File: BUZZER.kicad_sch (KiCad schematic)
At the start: 4 parts, among them Q1 AO3400A, U10 ZX-SH1.0-3PWT

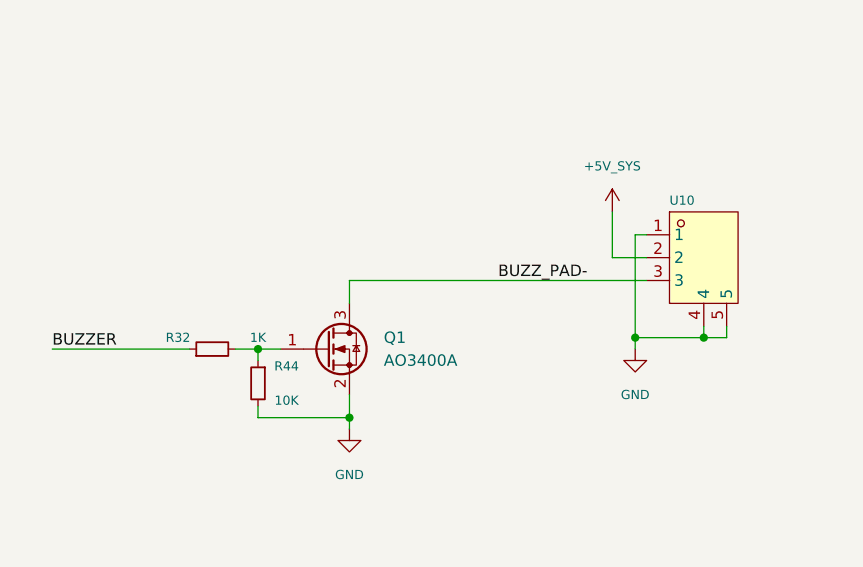
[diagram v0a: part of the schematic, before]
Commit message: grouped ICs and passives
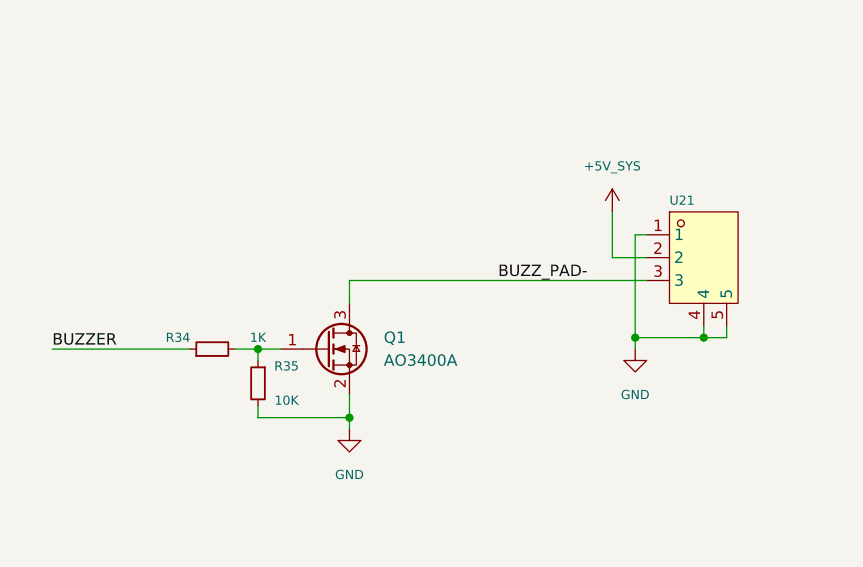
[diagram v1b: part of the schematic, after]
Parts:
- renumbered R32 to R34, R44 to R35, U10 to U21
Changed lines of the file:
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@@
 		(dnp no)
 		(fields_autoplaced yes)
-		(property "Reference" "#PWR0128"
+		(property "Reference" "#PWR0114"
 			(at 135.89 68.58 0)
 			(hide yes)
@@
 			(project "LEVIA_H7"
 				(path "/6b768b36-fce6-4be0-9021-6d41bddc3a70/40acc3ff-a355-41ce-95b6-fe5d468e4bb9"
-					(reference "#PWR0128")
+					(reference "#PWR0114")
 					(unit 1)
 				)
@@
 		(in_pos_files yes)
 		(dnp no)
-		(property "Reference" "R44"
+		(property "Reference" "R35"
 			(at 97.155 64.135 0)
 			(show_name no)
@@
 			(project "LEVIA_H7"
 				(path "/6b768b36-fce6-4be0-9021-6d41bddc3a70/40acc3ff-a355-41ce-95b6-fe5d468e4bb9"
-					(reference "R44")
+					(reference "R35")
 					(unit 1)
 				)
@@
 		(dnp no)
 		(fields_autoplaced yes)
-		(property "Reference" "#PWR085"
+		(property "Reference" "#PWR0112"
 			(at 104.14 77.47 0)
 			(hide yes)
@@
 			(project "LEVIA_H7"
 				(path "/6b768b36-fce6-4be0-9021-6d41bddc3a70/40acc3ff-a355-41ce-95b6-fe5d468e4bb9"
-					(reference "#PWR085")
+					(reference "#PWR0112")
 					(unit 1)
 				)
@@
 		(in_pos_files yes)
 		(dnp no)
-		(property "Reference" "R32"
+		(property "Reference" "R34"
 			(at 85.09 60.96 90)
 			(show_name no)
@@
 			(project "LEVIA_H7"
 				(path "/6b768b36-fce6-4be0-9021-6d41bddc3a70/40acc3ff-a355-41ce-95b6-fe5d468e4bb9"
-					(reference "R32")
+					(reference "R34")
 					(unit 1)
 				)
@@
 		(dnp no)
 		(fields_autoplaced yes)
-		(property "Reference" "#PWR062"
+		(property "Reference" "#PWR0113"
 			(at 133.35 50.8 0)
 			(hide yes)
@@
 			(project "LEVIA_H7"
 				(path "/6b768b36-fce6-4be0-9021-6d41bddc3a70/40acc3ff-a355-41ce-95b6-fe5d468e4bb9"
-					(reference "#PWR062")
+					(reference "#PWR0113")
 					(unit 1)
 				)
@@
 		(in_pos_files yes)
 		(dnp no)
-		(property "Reference" "U10"
+		(property "Reference" "U21"
 			(at 139.7 45.72 0)
 			(show_name no)
@@
 			(project "LEVIA_H7"
 				(path "/6b768b36-fce6-4be0-9021-6d41bddc3a70/40acc3ff-a355-41ce-95b6-fe5d468e4bb9"
-					(reference "U10")
-					(unit 1)
-				)
+					(reference "U21")
+					(unit 1)
+				)
